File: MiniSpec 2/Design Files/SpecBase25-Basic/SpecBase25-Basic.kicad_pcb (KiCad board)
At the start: 2 copper layers, 48 x 30 mm, 3 parts, among them J1 M20-8770642R, J2 M20-8770642R, J3 Conn_01x04_Male

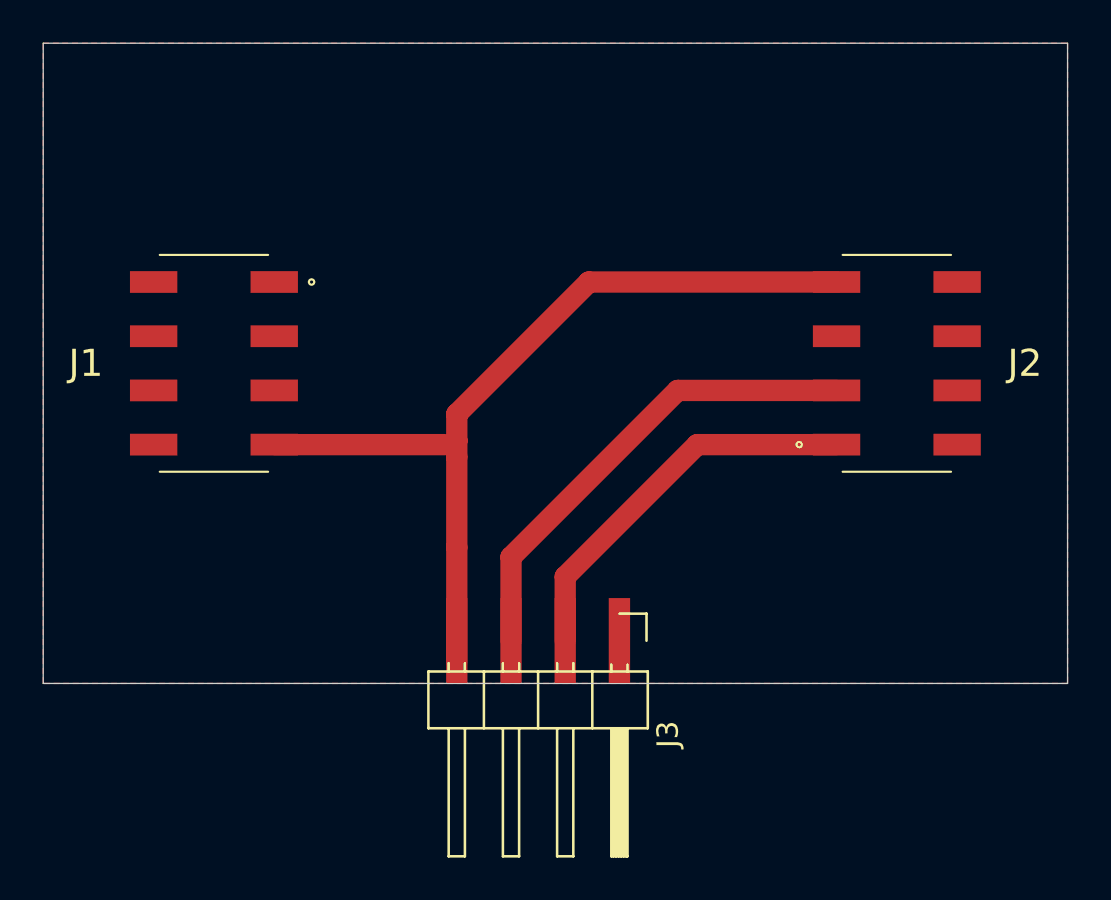
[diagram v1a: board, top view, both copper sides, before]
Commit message: big updates for 2 layer design with vias
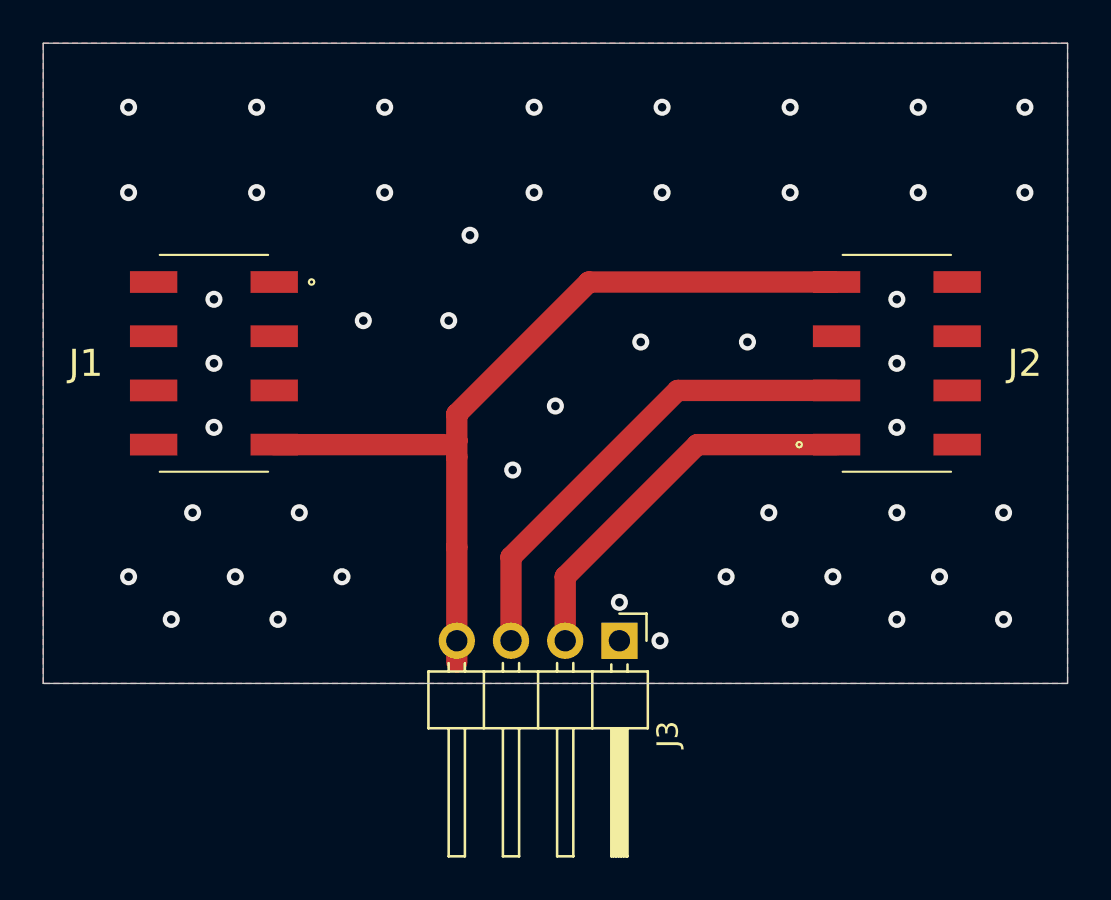
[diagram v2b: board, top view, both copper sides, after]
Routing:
- net GND: vias 0 -> 47
- added copper zone on B.Cu, net GND
